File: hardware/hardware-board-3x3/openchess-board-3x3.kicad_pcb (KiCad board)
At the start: 2 copper layers, 132 x 132 mm, 46 parts, among them J1 Conn_02x13, U1 DRV5032FC, U2 DRV5032FC, U3 DRV5032FC, U4 DRV5032FC, U5 DRV5032FC, U6 DRV5032FC, U7 DRV5032FC, U8 DRV5032FC, U9 DRV5032FC

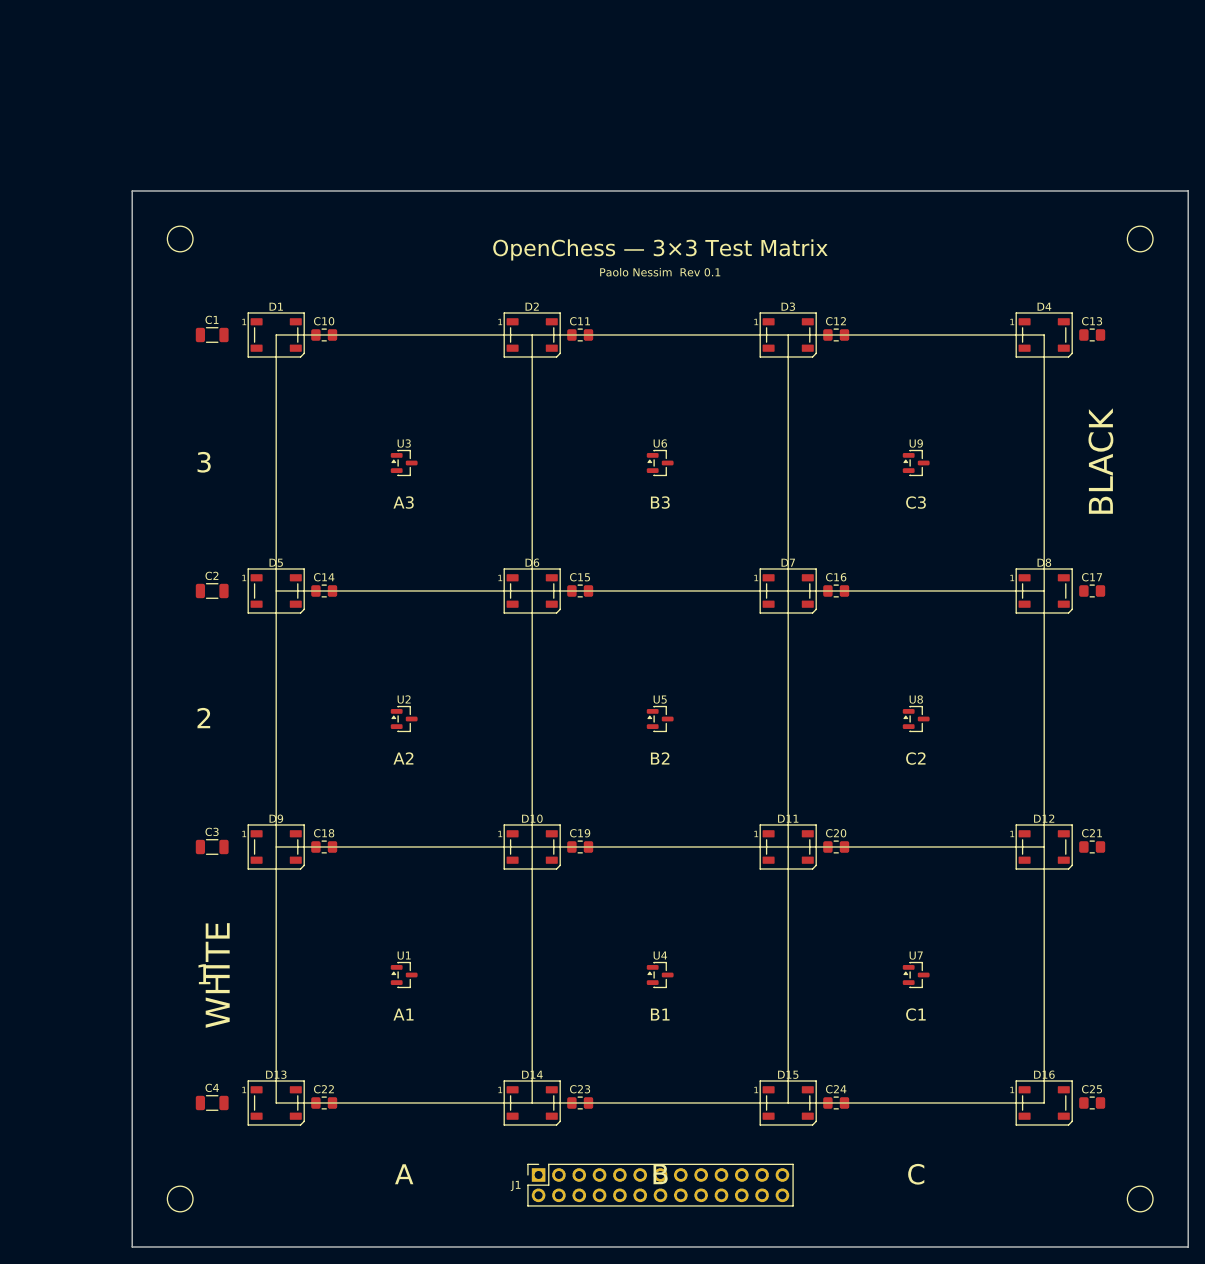
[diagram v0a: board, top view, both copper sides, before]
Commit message: Add scripts to merge and tile PDF layers for KiCad projects
- Implemented `merge_pdf_layers.py` to overlay multiple single-page PDFs into one page, allowing for easy printing of layered designs.
- Created `tile_pdf_to_a4.py` to split large PDFs into A4-sized tiles with configurable overlap, facilitating printing on standard home printers.
- Both scripts require the `pypdf` library for PDF manipulation.
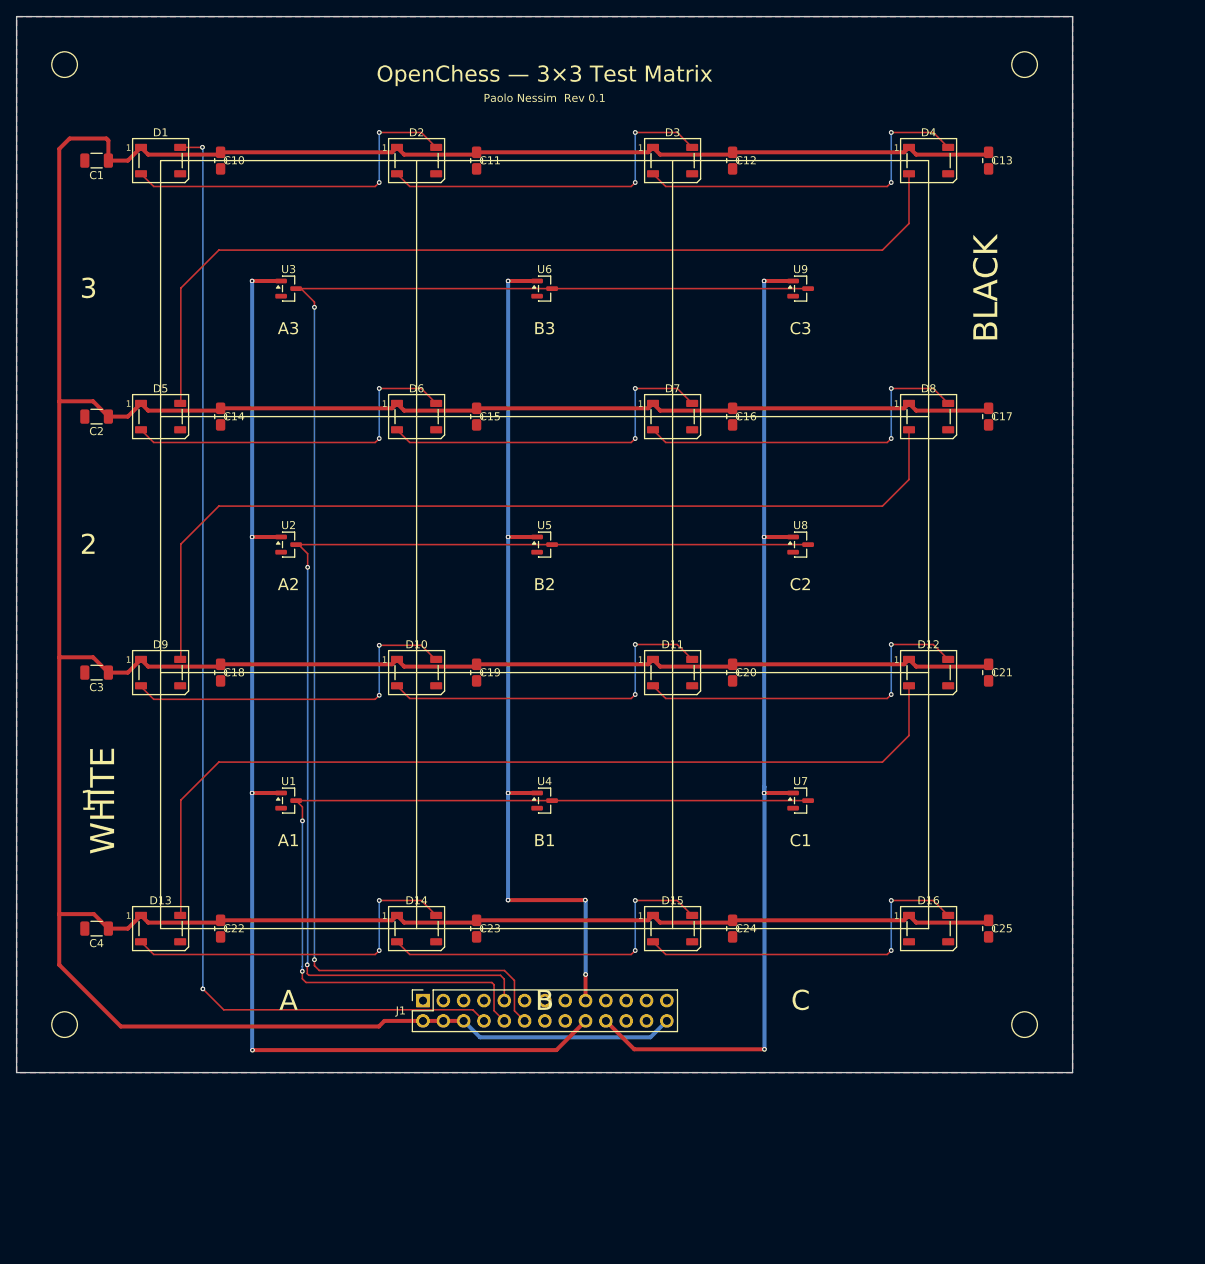
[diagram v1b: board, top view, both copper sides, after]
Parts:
- moved C1 26.2 mm to (45.6, 46.2), turned to 180 degrees
- moved D1 26.2 mm to (53.6, 46.2)
- moved C2 26.2 mm to (45.6, 78.2), turned to 180 degrees
- moved C3 26.2 mm to (45.6, 110.2), turned to 180 degrees
- moved C4 26.2 mm to (45.6, 142.2), turned to 180 degrees
- moved D13 26.2 mm to (53.6, 142.2)
- moved D2 26.2 mm to (85.6, 46.2)
- moved D3 26.2 mm to (117.6, 46.2)
- moved D4 26.2 mm to (149.6, 46.2)
- moved D5 26.2 mm to (53.6, 78.2)
- moved D9 26.2 mm to (53.6, 110.2)
- moved U3 26.2 mm to (69.6, 62.2)
- moved U6 26.2 mm to (101.6, 62.2)
- moved U9 26.2 mm to (133.6, 62.2)
- moved D10 26.2 mm to (85.6, 110.2)
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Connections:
- J1 pad 1: +5V_LED -> GND
- J1 pad 10: /S1 -> /S0
- J1 pad 11: /S2 -> /S3
- J1 pad 12: /S3 -> /S2
- J1 pad 13: /S4 -> /S5
- J1 pad 14: /S5 -> /S4
- J1 pad 15: /S6 -> /S7
- J1 pad 16: /S7 -> /S6
- J1 pad 17: /CA_PWR -> /CB_PWR
- J1 pad 18: /CB_PWR -> /CA_PWR
- J1 pad 19: /CC_PWR -> /CD_PWR
- J1 pad 2: GND -> +5V_LED
- J1 pad 20: /CD_PWR -> /CC_PWR
- J1 pad 21: /CE_PWR -> /CF_PWR
- J1 pad 22: /CF_PWR -> /CE_PWR
- J1 pad 23: /CG_PWR -> /CH_PWR
- J1 pad 24: /CH_PWR -> /CG_PWR
- J1 pad 25: +5V_LED -> GND
- J1 pad 26: GND -> +5V_LED
- J1 pad 3: +5V_LED -> GND
- J1 pad 4: GND -> +5V_LED
- J1 pad 5: +5V_LED -> GND
- J1 pad 6: GND -> +5V_LED
- J1 pad 7: /LED_DATA_5V -> GND
- J1 pad 8: GND -> /LED_DATA_5V
- J1 pad 9: /S0 -> /S1
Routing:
- net +5V_LED: track 0.00 -> 666.9 mm
- net /S2: track 0.00 -> 181.3 mm, vias 0 -> 2
- net /CA_PWR: track 0.00 -> 150.2 mm, vias 0 -> 4
- net /S1: track 0.00 -> 146.0 mm, vias 0 -> 2
- net /LED_DATA_5V: track 0.00 -> 144.8 mm, vias 0 -> 2
- net /CC_PWR: track 0.00 -> 129.0 mm, vias 0 -> 4
- net /S0: track 0.00 -> 115.9 mm, vias 0 -> 2
- net /L12: track 0.00 -> 115.0 mm
- net /L8: track 0.00 -> 115.0 mm
- net /L4: track 0.00 -> 115.0 mm
- net /CB_PWR: track 0.00 -> 110.5 mm, vias 0 -> 6
- net Net-(D10-DIN): track 0.00 -> 44.8 mm, vias 0 -> 2
- net Net-(D7-DOUT): track 0.00 -> 44.8 mm, vias 0 -> 2
- net Net-(D6-DOUT): track 0.00 -> 44.8 mm, vias 0 -> 2
- net Net-(D5-DOUT): track 0.00 -> 44.8 mm, vias 0 -> 2
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- added copper zone on B.Cu, net GND
- added copper zone on F.Cu, net GND

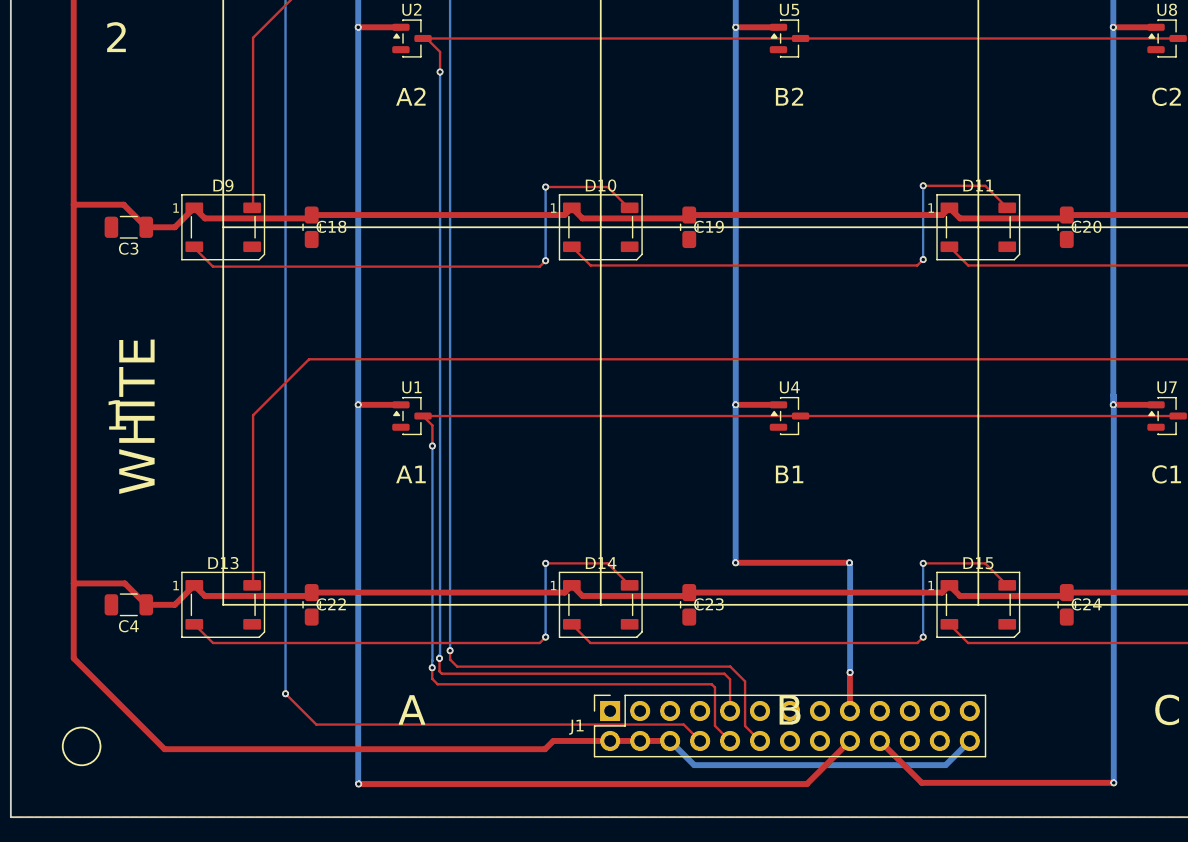
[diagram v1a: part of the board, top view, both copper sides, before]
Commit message: chore: update code structure and remove redundant sections
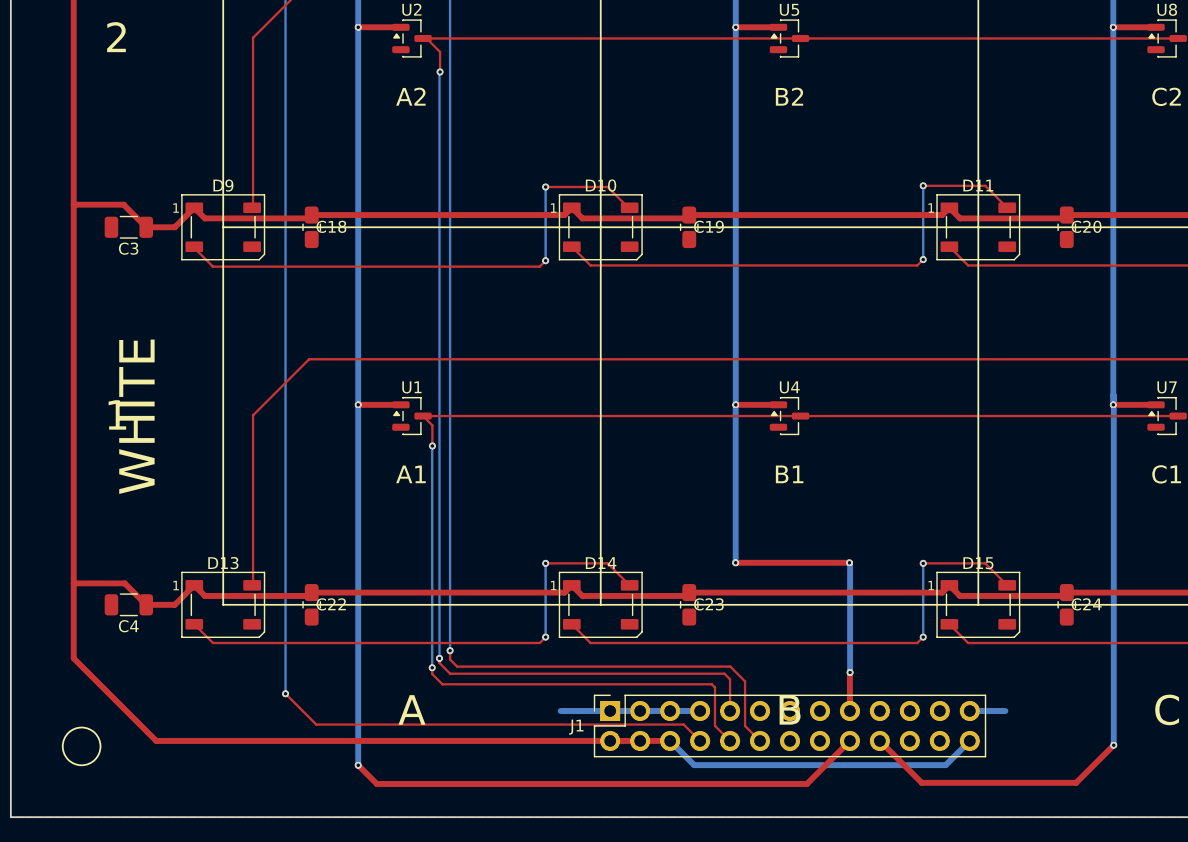
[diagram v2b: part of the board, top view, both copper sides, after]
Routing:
- net GND: track 0.00 -> 14.8 mm
- net /CC_PWR: track 129.0 -> 127.1 mm
- net /CA_PWR: track 150.2 -> 149.3 mm
- net +5V_LED: track 666.9 -> 666.4 mm
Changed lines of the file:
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@@
+	)
+	(segment
+		(start 40.8815 146.738)
+		(end 40.8815 140.388)
+		(width 0.5)
+		(layer "F.Cu")
+		(net "+5V_LED")
 	)
 	(segment
@@
 	)
 	(segment
+		(start 91.43025 153.7405)
+		(end 47.884 153.7405)
+		(width 0.5)
+		(layer "F.Cu")
+		(net "+5V_LED")
+	)
+	(segment
 		(start 49.45025 78.2005)
 		(end 51.10025 76.5505)
@@
 	)
 	(segment
-		(start 48.5815 154.438)
-		(end 40.8815 146.738)
-		(width 0.5)
-		(layer "F.Cu")
-		(net "+5V_LED")
-	)
-	(segment
 		(start 147.10025 76.5505)
 		(end 148.00025 77.4505)
@@
 	)
 	(segment
-		(start 81.529 153.7405)
-		(end 91.43025 153.7405)
-		(width 0.5)
-		(layer "F.Cu")
-		(net "+5V_LED")
-	)
-	(segment
 		(start 82.48775 77.163)
 		(end 83.10025 76.5505)
@@
 	)
 	(segment
+		(start 47.884 153.7405)
+		(end 40.8815 146.738)
+		(width 0.5)
+		(layer "F.Cu")
+		(net "+5V_LED")
+	)
+	(segment
 		(start 148.00025 45.4505)
 		(end 156.76275 45.4505)
@@
 	)
 	(segment
-		(start 40.8815 146.738)
-		(end 40.8815 140.388)
-		(width 0.5)
-		(layer "F.Cu")
-		(net "+5V_LED")
-	)
-	(segment
 		(start 47.02525 78.2005)
 		(end 45.11275 76.288)
@@
 	)
 	(segment
-		(start 80.8315 154.438)
-		(end 48.5815 154.438)
-		(width 0.5)
-		(layer "F.Cu")
-		(net "+5V_LED")
-	)
-	(segment
 		(start 84.00025 45.4505)
 		(end 92.76275 45.4505)
@@
 	)
 	(segment
-		(start 80.8315 154.438)
-		(end 81.529 153.7405)
-		(width 0.5)
-		(layer "F.Cu")
-		(net "+5V_LED")
-	)
-	(segment
 		(start 93.47775 155.788)
 		(end 91.43025 153.7405)
@@
 	)
 	(segment
+		(start 116.83025 151.2005)
+		(end 119.85025 151.2005)
+		(width 0.5)
+		(layer "B.Cu")
+		(net "GND")
+	)
+	(segment
+		(start 93.97025 151.2005)
+		(end 82.15025 151.2005)
+		(width 0.5)
+		(layer "B.Cu")
+		(net "GND")
+	)
+	(segment
 		(start 68.61275 93.2505)
 		(end 64.99375 93.2505)
@@
 	)
 	(segment
-		(start 106.67025 153.7405)
-		(end 103.02275 157.388)
+		(start 103.02275 157.388)
+		(end 106.67025 153.7405)
+		(width 0.5)
+		(layer "F.Cu")
+		(net "/CA_PWR")
+	)
+	(segment
+		(start 64.99375 155.8005)
+		(end 66.58125 157.388)
 		(width 0.5)
 		(layer "F.Cu")
@@
 	)
 	(segment
-		(start 103.02275 157.388)
-		(end 65.0315 157.388)
+		(start 66.58125 157.388)
+		(end 103.02275 157.388)
 		(width 0.5)
 		(layer "F.Cu")
@@
 	)
 	(via
-		(at 65.0315 157.388)
+		(at 64.99375 155.8005)
 		(size 0.6)
 		(drill 0.3)
@@
 		(drill 0.3)
 		(layers "F.Cu" "B.Cu")
-		(net "/CA_PWR")
-	)
-	(segment
-		(start 65.0315 157.388)
-		(end 64.99375 157.35025)
-		(width 0.5)
-		(layer "B.Cu")
 		(net "/CA_PWR")
 	)
@@
 	)
 	(segment
-		(start 64.99375 157.35025)
+		(start 64.99375 155.8005)
 		(end 64.99375 125.2505)
 		(width 0.5)
 		(layer "B.Cu")
 		(net "/CA_PWR")
-	)
-	(segment
-		(start 71.8815 146.7375)
-		(end 71.8815 147.838)
-		(width 0.2)
-		(layer "F.Cu")
-		(net "/S1")
 	)
 	(segment
@@
 	)
 	(segment
-		(start 72.0815 148.038)
+		(start 96.51025 148.51675)
+		(end 96.51025 151.2005)
+		(width 0.2)
+		(layer "F.Cu")
+		(net "/S1")
+	)
+	(segment
+		(start 71.8815 147.13175)
+		(end 72.78775 148.038)
+		(width 0.2)
+		(layer "F.Cu")
+		(net "/S1")
+	)
+	(segment
+		(start 71.8815 146.7375)
+		(end 71.8815 147.13175)
+		(width 0.2)
+		(layer "F.Cu")
+		(net "/S1")
+	)
+	(segment
+		(start 72.78775 148.038)
 		(end 96.0315 148.038)
-		(width 0.2)
-		(layer "F.Cu")
-		(net "/S1")
-	)
-	(segment
-		(start 71.8815 147.838)
-		(end 72.0815 148.038)
 		(width 0.2)
 		(layer "F.Cu")
@@
 	)
 	(segment
-		(start 96.51025 148.51675)
-		(end 96.51025 151.2005)
+		(start 96.0315 148.038)
+		(end 96.51025 148.51675)
 		(width 0.2)
 		(layer "F.Cu")
@@
 		(net "/S1")
 	)
-	(segment
-		(start 96.0315 148.038)
-		(end 96.51025 148.51675)
-		(width 0.2)
-		(layer "F.Cu")
+	(via
+		(at 71.9315 97.038)
+		(size 0.6)
+		(drill 0.3)
+		(layers "F.Cu" "B.Cu")
 		(net "/S1")
 	)
 	(via
-		(at 71.9315 97.038)
+		(at 71.8815 146.7375)
 		(size 0.6)
 		(drill 0.3)
@@
 		(net "/S1")
 	)
-	(via
-		(at 71.8815 146.7375)
-		(size 0.6)
-		(drill 0.3)
-		(layers "F.Cu" "B.Cu")
+	(segment
+		(start 71.8815 97.088)
+		(end 71.9315 97.038)
+		(width 0.2)
+		(layer "B.Cu")
 		(net "/S1")
 	)
 	(segment
-		(start 71.9315 146.388)
-		(end 71.9315 97.038)
-		(width 0.2)
-		(layer "B.Cu")
-		(net "/S1")
-	)
-	(segment
 		(start 71.8815 146.7375)
-		(end 71.8815 146.438)
-		(width 0.2)
-		(layer "B.Cu")
-		(net "/S1")
-	)
-	(segment
-		(start 71.8815 146.438)
-		(end 71.9315 146.388)
+		(end 71.8815 97.088)
 		(width 0.2)
 		(layer "B.Cu")
@@
 	)
 	(segment
-		(start 109.21025 153.7405)
-		(end 112.75775 157.288)
+		(start 112.75775 157.288)
+		(end 109.21025 153.7405)
 		(width 0.5)
 		(layer "F.Cu")
@@
 	)
 	(segment
-		(start 112.75775 157.288)
-		(end 129.0315 157.288)
+		(start 129.0315 154.1005)
+		(end 125.844 157.288)
 		(width 0.5)
 		(layer "F.Cu")
 		(net "/CC_PWR")
 	)
+	(segment
+		(start 125.844 157.288)
+		(end 112.75775 157.288)
+		(width 0.5)
+		(layer "F.Cu")
+		(net "/CC_PWR")
+	)
 	(via
 		(at 128.99375 125.2505)
@@
 	)
 	(via
-		(at 129.0315 157.288)
+		(at 129.0315 154.1005)
 		(size 0.6)
 		(drill 0.3)
@@
 	)
 	(segment
-		(start 129.0315 157.288)
+		(start 129.0315 154.1005)
 		(end 129.0315 124.47575)
 		(width 0.5)
@@
 	)
 	(segment
+		(start 72.13775 148.938)
+		(end 94.959 148.938)
+		(width 0.2)
+		(layer "F.Cu")
+		(net "/S0")
+	)
+	(segment
+		(start 95.2315 152.46175)
+		(end 96.51025 153.7405)
+		(width 0.2)
+		(layer "F.Cu")
+		(net "/S0")
+	)
+	(segment
 		(start 94.959 148.938)
 		(end 95.2315 149.2105)
@@
 	)
 	(segment
-		(start 71.7315 148.938)
-		(end 94.959 148.938)
-		(width 0.2)
-		(layer "F.Cu")
-		(net "/S0")
-	)
-	(segment
-		(start 71.266921 148.473421)
-		(end 71.7315 148.938)
-		(width 0.2)
-		(layer "F.Cu")
-		(net "/S0")
-	)
-	(segment
 		(start 71.2815 126.99425)
 		(end 70.48775 126.2005)
@@
 	)
 	(segment
+		(start 71.266921 148.067171)
+		(end 72.13775 148.938)
+		(width 0.2)
+		(layer "F.Cu")
+		(net "/S0")
+	)
+	(segment
+		(start 71.266921 147.5375)
+		(end 71.266921 148.067171)
+		(width 0.2)
+		(layer "F.Cu")
+		(net "/S0")
+	)
+	(segment
+		(start 70.48775 126.2005)
+		(end 134.48775 126.2005)
+		(width 0.2)
+		(layer "F.Cu")
+		(net "/S0")
+	)
+	(segment
+		(start 71.2815 128.738)
+		(end 71.2815 126.99425)
+		(width 0.2)
+		(layer "F.Cu")
+		(net "/S0")
+	)
+	(segment
 		(start 95.2315 149.2105)
 		(end 95.2315 152.46175)
@@
 		(net "/S0")
 	)
-	(segment
-		(start 95.2315 152.46175)
-		(end 96.51025 153.7405)
-		(width 0.2)
-		(layer "F.Cu")
+	(via
+		(at 71.266921 147.5375)
+		(size 0.6)
+		(drill 0.3)
+		(layers "F.Cu" "B.Cu")
 		(net "/S0")
 	)
+	(via
+		(at 71.2815 128.738)
+		(size 0.6)
+		(drill 0.3)
+		(layers "F.Cu" "B.Cu")
+		(net "/S0")
+	)
 	(segment
 		(start 71.266921 147.5375)
-		(end 71.266921 148.473421)
-		(width 0.2)
-		(layer "F.Cu")
+		(end 71.266921 128.752579)
+		(width 0.2)
+		(layer "B.Cu")
 		(net "/S0")
 	)
 	(segment
-		(start 70.48775 126.2005)
-		(end 134.48775 126.2005)
-		(width 0.2)
-		(layer "F.Cu")
-		(net "/S0")
-	)
-	(segment
-		(start 71.2815 128.738)
-		(end 71.2815 126.99425)
-		(width 0.2)
-		(layer "F.Cu")
-		(net "/S0")
-	)
-	(via
-		(at 71.266921 147.5375)
-		(size 0.6)
-		(drill 0.3)
-		(layers "F.Cu" "B.Cu")
-		(net "/S0")
-	)
-	(via
-		(at 71.2815 128.738)
-		(size 0.6)
-		(drill 0.3)
-		(layers "F.Cu" "B.Cu")
-		(net "/S0")
-	)
-	(segment
-		(start 71.266921 146.950149)
-		(end 71.2815 146.93557)
-		(width 0.2)
-		(layer "B.Cu")
-		(net "/S0")
-	)
-	(segment
-		(start 71.266921 147.5375)
-		(end 71.266921 146.950149)
-		(width 0.2)
-		(layer "B.Cu")
-		(net "/S0")
-	)
-	(segment
-		(start 71.2815 146.93557)
+		(start 71.266921 128.752579)
 		(end 71.2815 128.738)
 		(width 0.2)

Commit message: Refactor code structure for improved readability and maintainability
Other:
- board text removed: "1"
- board text removed: "B"
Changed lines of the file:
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@@
 			(pdf_back_fp_property_popups yes)
 			(pdf_metadata yes)
-			(pdf_single_document yes)
+			(pdf_single_document no)
 			(dxfpolygonmode yes)
 			(dxfimperialunits yes)
@@
 			(crossoutdnponfab yes)
 			(subtractmaskfromsilk no)
-			(outputformat 4)
+			(outputformat 1)
 			(mirror no)
 			(drillshape 0)
 			(scaleselection 1)
-			(outputdirectory "images")
+			(outputdirectory "gerbers")
 		)
 	)
@@
 		)
 	)
-	(gr_text "1"
-		(at 44.55025 126.2005 0)
-		(layer "F.SilkS")
-		(effects
-			(font
-				(size 2.5 2.5)
-				(thickness 0.3)
-			)
-		)
-	)
 	(gr_text "A"
 		(at 69.55025 151.2005 0)
 		(layer "F.SilkS")
 		(effects
-			(font
-				(size 2.5 2.5)
-				(thickness 0.3)
-			)
-		)
-	)
-	(gr_text "B"
-		(at 101.55025 151.2005 0)
-		(layer "F.SilkS")
-		(effects
